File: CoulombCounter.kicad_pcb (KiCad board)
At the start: 2 copper layers, 39.4 x 34.3 mm, 14 parts, among them J1 Screw_Terminal_01x02, J2 Screw_Terminal_01x02, J3 Screw_Terminal_01x02, J4 Conn_01x05_Male, U1 LTC2943

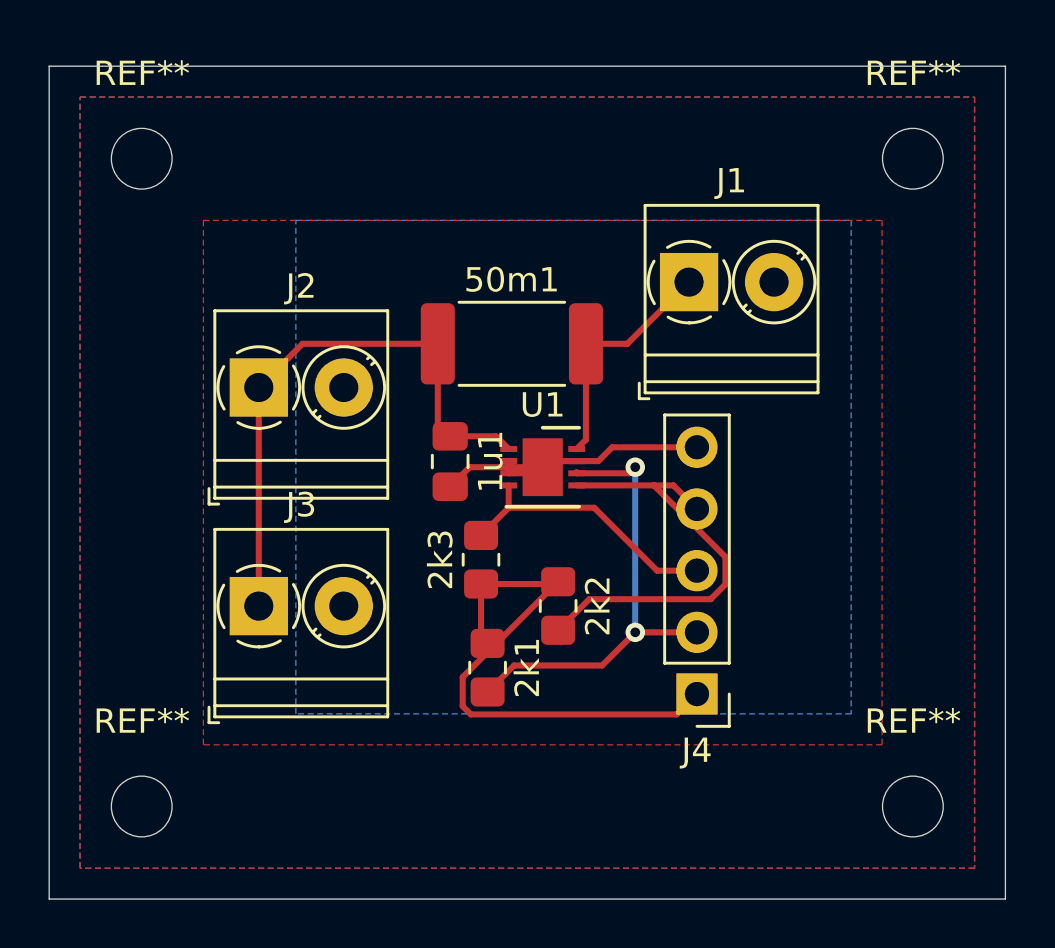
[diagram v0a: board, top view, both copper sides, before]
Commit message: Fixed shorting PWR and GND, references and values, and silkscreen
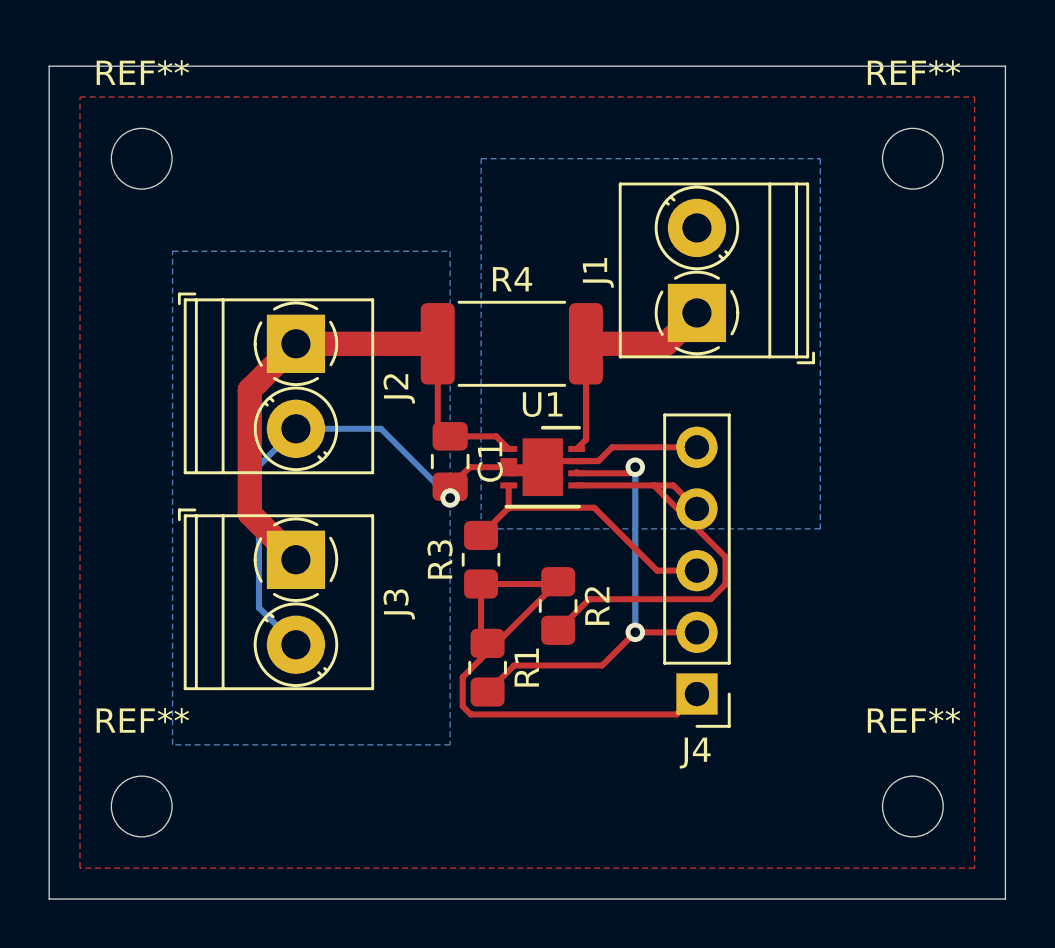
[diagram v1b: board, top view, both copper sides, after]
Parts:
- added ?: , , F.Cu at (165.1, 47.0)
- C1: renamed from 1u1; value C1 -> 1u
- R1: renamed from 2k1; value R1 -> 2k
- R2: renamed from 2k2; value R2 -> 2k
- R3: renamed from 2k3; value R3 -> 2k
- R4: renamed from 50m1; value R4 -> 50m
- moved J3 2.45 mm to (144.8, 53.3), turned to 270 degrees
- moved J2 2.36 mm to (144.8, 44.5), turned to 270 degrees
- moved J1 1.31 mm to (161.3, 43.2), turned to 90 degrees
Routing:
- net GND: track 12.9 -> 30.6 mm, vias 0 -> 1
- net Net-(C1-Pad1): track 23.8 -> 23.0 mm
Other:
- board text added: "Conn_01x05_Male"

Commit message: Added silkscreen
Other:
- board text added: "Coulomb Counter Husky Satellite Lab 2020 Designed by Katharine Lundblad"
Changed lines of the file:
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@@
   (general
     (thickness 1.6)
-    (drawings 5)
+    (drawings 6)
     (tracks 63)
     (zones 0)
@@
     )
   )
+  (gr_text "Coulomb Counter\nHusky Satellite Lab 2020\nDesigned by Katharine Lundblad" (at 153.67 48.26) (layer B.SilkS)
+    (effects (font (size 1 1) (thickness 0.15)) (justify mirror))
+  )
   (gr_text Conn_01x05_Male (at 161.29 60.96) (layer F.Fab)
